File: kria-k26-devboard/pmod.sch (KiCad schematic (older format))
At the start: 7 parts, among them J4 SSW-106-02-G-D-RA, U14 TPD4E05U06QDQARQ1, U15 TPD4E05U06QDQARQ1

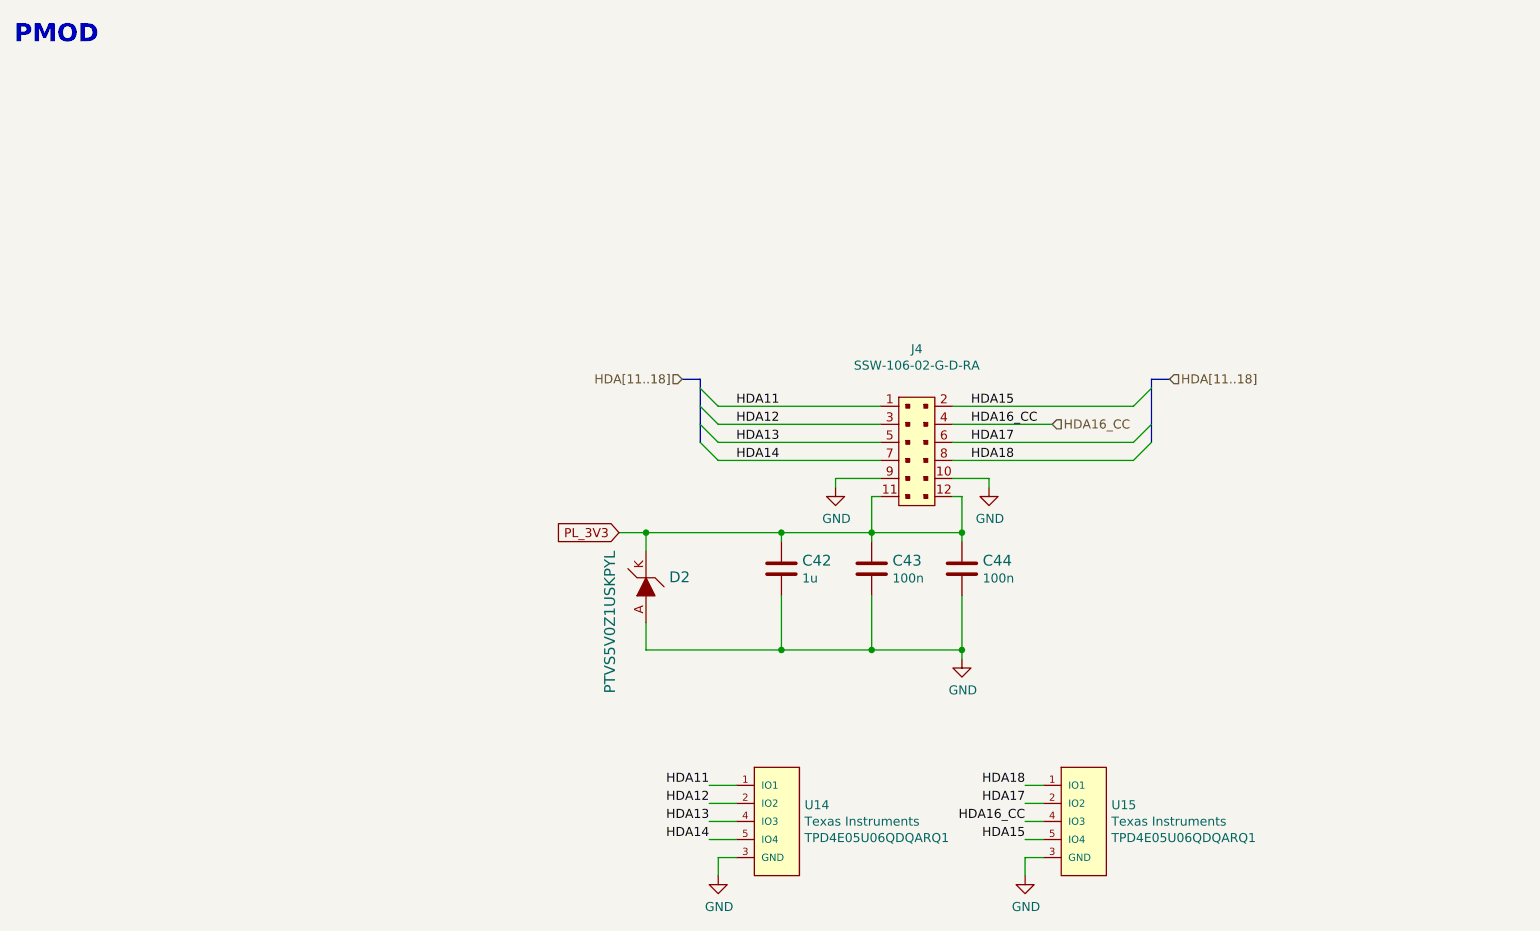
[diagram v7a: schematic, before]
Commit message: Fixes introduced after initial review, length matching double checked with external plugin
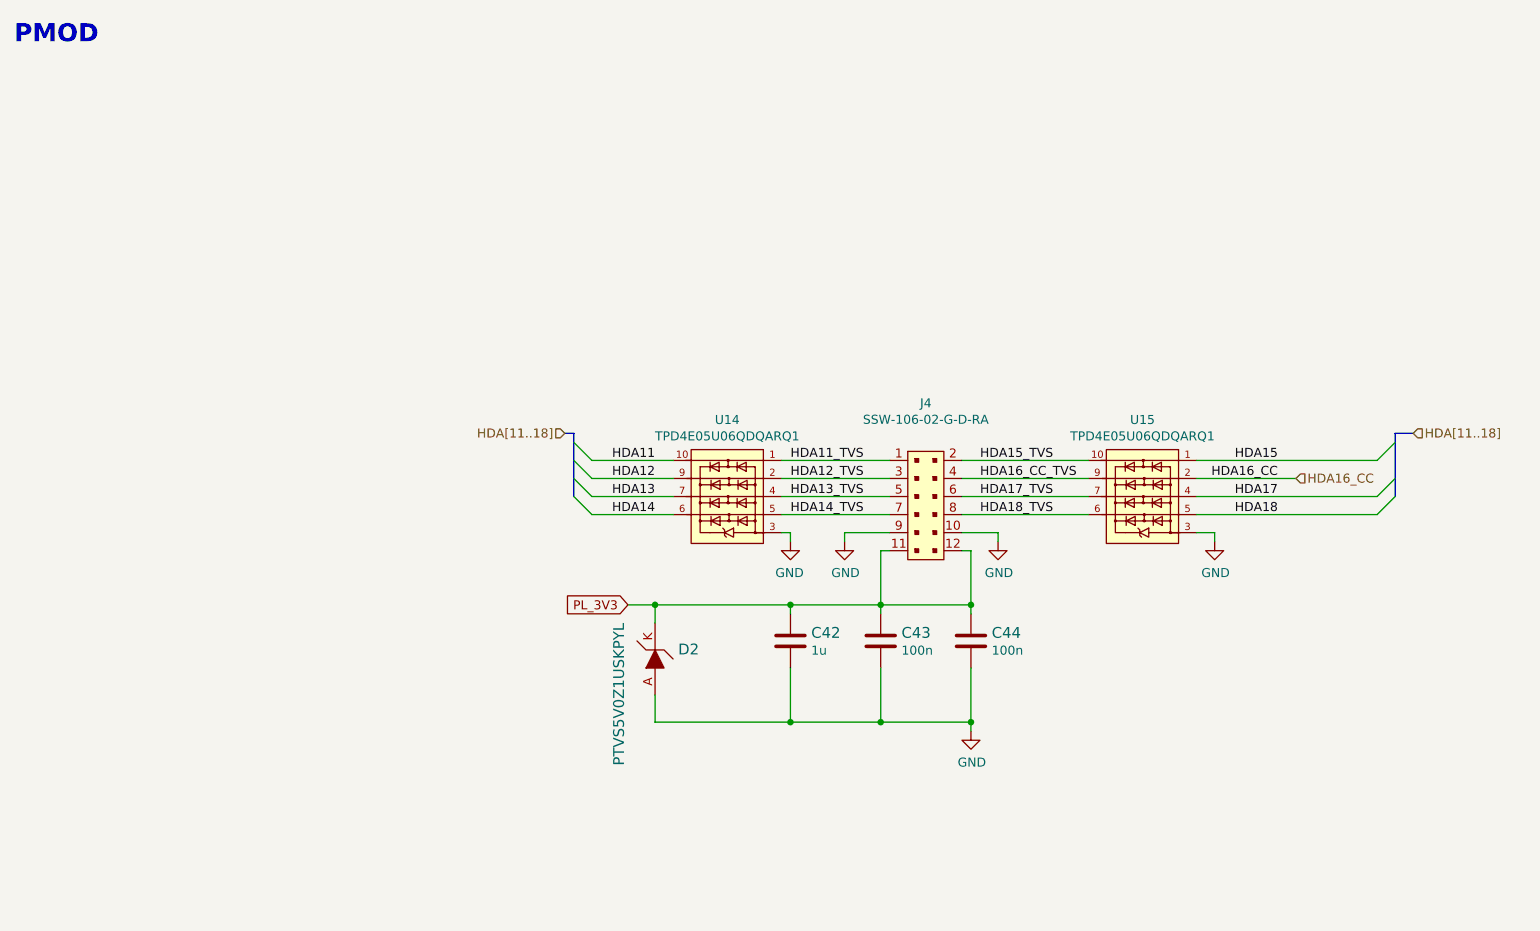
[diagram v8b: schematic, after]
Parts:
- removed U14, U15: TPD4E05U06QDQARQ1, antmicro-footprints:TPD4E05U06QDQARQ1, symbol antmicroTVSDiodes:TPD4E05U06QDQARQ1
- added U14, U15: TPD4E05U06QDQARQ1_PASS, antmicro-footprints:TPD4E05U06QDQARQ1, symbol antmicroTVSDiodes:TPD4E05U06QDQARQ1_PASS
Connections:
- net GND: now also U14.3, U14.8 (GND), U15.3, U15.8 (GND)
- net HDA11: now also U14.10; no longer J4.1
- net HDA12: now also U14.9; no longer J4.3
- net HDA13: now also U14.7; no longer J4.5
- net HDA14: now also U14.6; no longer J4.7
- net HDA15: now also U15.1; no longer J4.2
- net HDA16_CC: now also U15.2; no longer J4.4
- net HDA17: now also U15.4; no longer J4.6
- net HDA18: now also U15.5; no longer J4.8
- new net HDA11_TVS: J4.1, U14.1
- new net HDA12_TVS: J4.3, U14.2
- new net HDA13_TVS: J4.5, U14.4
- new net HDA14_TVS: J4.7, U14.5
- new net HDA15_TVS: J4.2, U15.10
- new net HDA16_CC_TVS: J4.4, U15.9
- new net HDA17_TVS: J4.6, U15.7
- new net HDA18_TVS: J4.8, U15.6
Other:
- moved on the sheet: C42, C43, C44, D2, J4
